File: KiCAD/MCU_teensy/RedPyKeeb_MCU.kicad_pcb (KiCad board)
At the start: 4 copper layers, 81 x 58 mm, 9 parts, among them J0 Conn_01x04, J1 Conn_02x20_Top_Bottom, J2 Conn_01x04, SW1 SW_DIP_x04, U0 Teensy4.1, U1 TXS0104ED

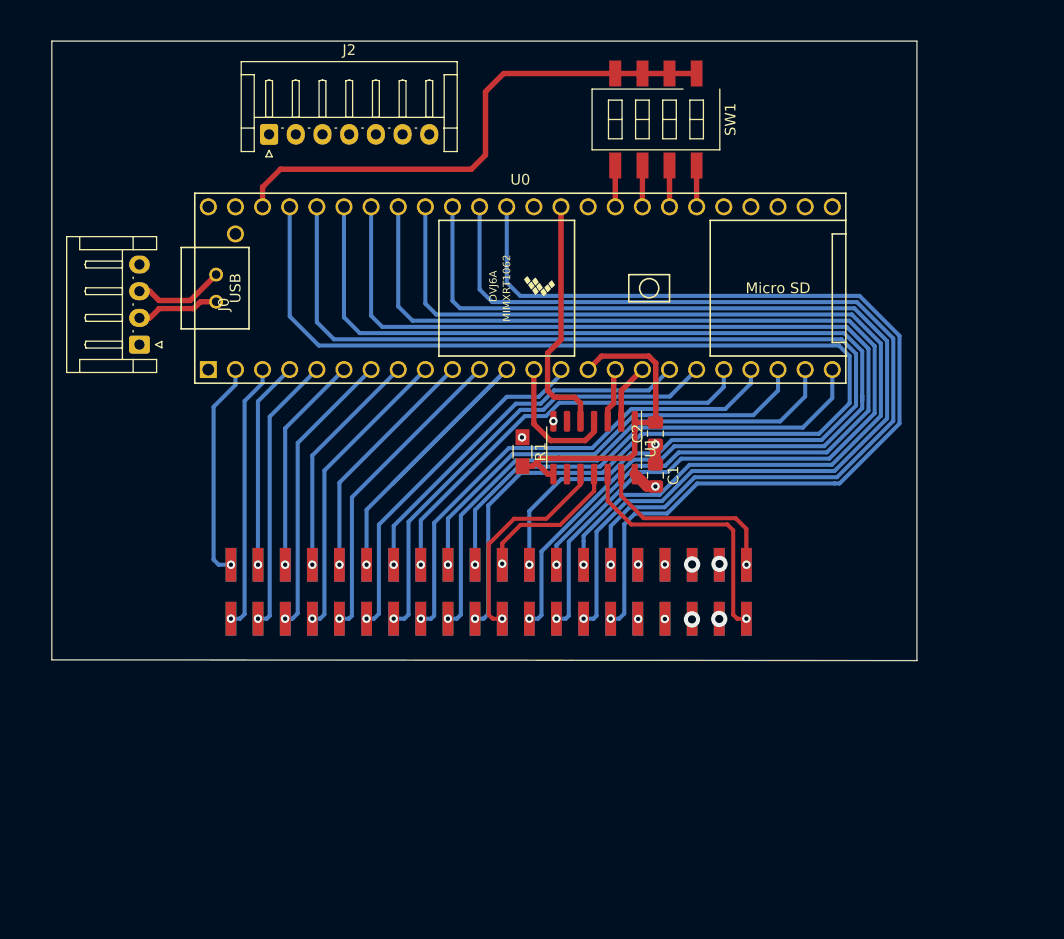
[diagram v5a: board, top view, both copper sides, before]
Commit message: Make more fixes and revisions to both PCBs, add in a pico for lighting and display functions and hook up an SPI bus with key event data.
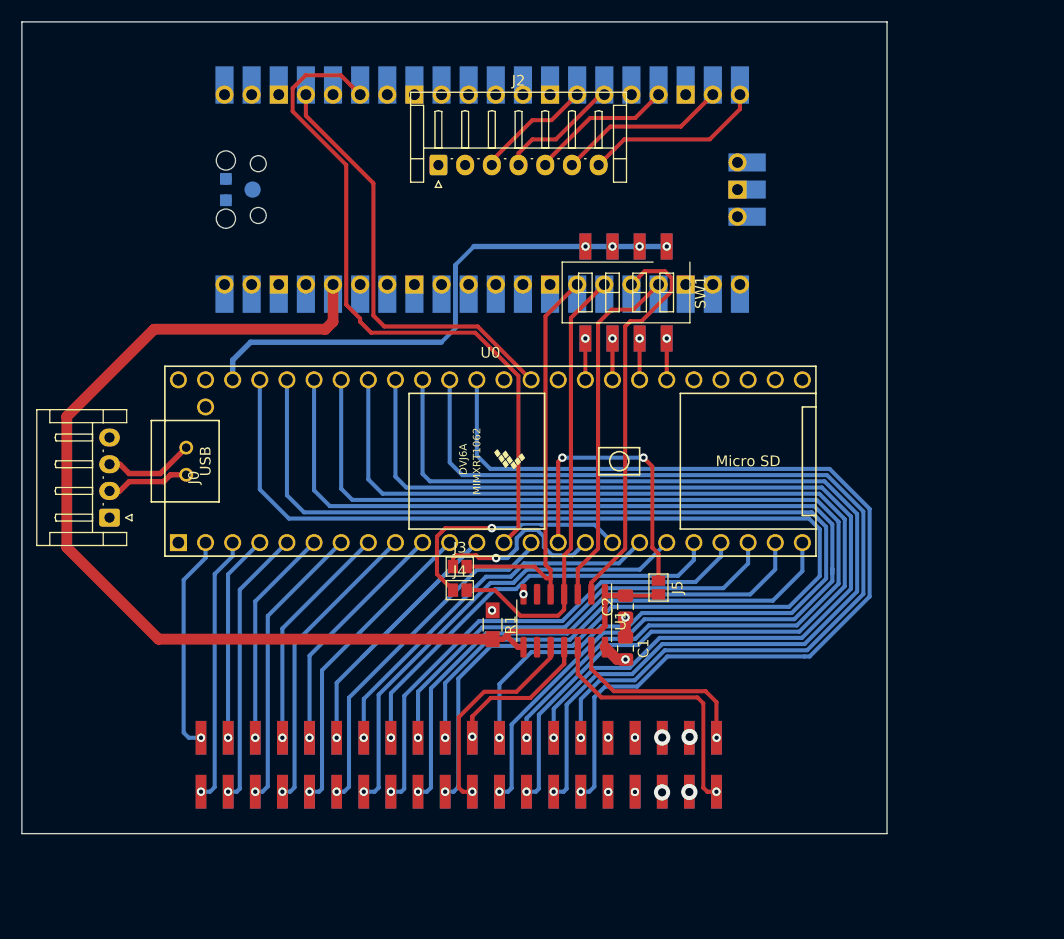
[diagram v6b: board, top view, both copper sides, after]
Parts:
- added J3: GS2, Connectors:GS2, F.Cu at (57.2, 66.2)
- added J4: GS2, Connectors:GS2, F.Cu at (57.2, 68.4)
- added J5: GS2, Connectors:GS2, F.Cu at (75.8, 68.2)
- added U2: Pico, Custom_pico:RPi_Pico_SMD_TH, B.Cu at (84.8, 20.4)
- SW1: footprint Buttons_Switches_SMD:SW_DIP_x4_W8.61mm_Slide_LowProfile -> Custom_pico:SW_DIP_x4_W8.61mm_Slide_LowProfile_bothsides
- moved C1 16.4 mm to (72.7, 73.9)
- moved J0 16.4 mm to (24.4, 61.6)
- moved J1 16.4 mm to (57.1, 84.8)
- moved R1 16.4 mm to (60.3, 71.6)
- moved U0 16.4 mm to (60.1, 56.3)
- moved U1 16.4 mm to (67.0, 71.3)
- moved SW1 16.4 mm to (72.8, 40.5)
- moved C2 16.4 mm to (72.7, 69.9)
- moved J2 16.1 mm to (55.2, 28.6)
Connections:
- C2 pad 2: 33_REF -> LED_33_REF
- R1 pad 2: 33_REF -> LED_33_REF
- U0 pad 13: LED_SDA_ROW0_MCU -> KEYS_MOSI
- U0 pad 16: LED_SCL_STATUS0_MCU -> Net-(J3-Pad1)
- U0 pad 17: LED_SDA_STATUS0_MCU -> Net-(J4-Pad1)
- U0 pad 35: LED_SCL_ROW0_MCU -> KEYS_CLK
- U0 pad 49: MAIN_VBUS -> Net-(U0-Pad49)
- U1 pad 1: 33_REF -> LED_33_REF
- U1 pad 8: 33_REF -> LED_33_REF
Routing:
- net LED_33_REF: track 0.00 -> 108.9 mm
- net KEYS_MOSI: track 0.00 -> 65.1 mm
- net KEYS_CLK: track 0.00 -> 40.6 mm
- net LED_SDA_STATUS0_MCU: track 5.66 -> 37.9 mm
- net LED_SDA_ROW0_MCU: track 12.7 -> 42.4 mm
- net LED_SCL_STATUS0_MCU: track 5.13 -> 33.3 mm
- net Net-(J4-Pad1): track 0.00 -> 23.2 mm, vias 0 -> 1
- net Net-(J3-Pad1): track 0.00 -> 17.1 mm, vias 0 -> 1
- net Net-(J2-Pad7): track 0.00 -> 16.8 mm
- net Net-(J2-Pad6): track 0.00 -> 15.9 mm
- net LED_SCL_ROW0_MCU: track 23.0 -> 38.7 mm
- net Net-(J2-Pad5): track 0.00 -> 13.5 mm
- net Net-(J2-Pad4): track 0.00 -> 11.4 mm
- net Net-(J2-Pad3): track 0.00 -> 11.0 mm
- net 33_REF_DIP: track 50.4 -> 56.3 mm, vias 0 -> 4
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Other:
- board size 81 x 58 mm -> 81 x 76 mm

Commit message: Allow for dual MCU for lighting/display and key management
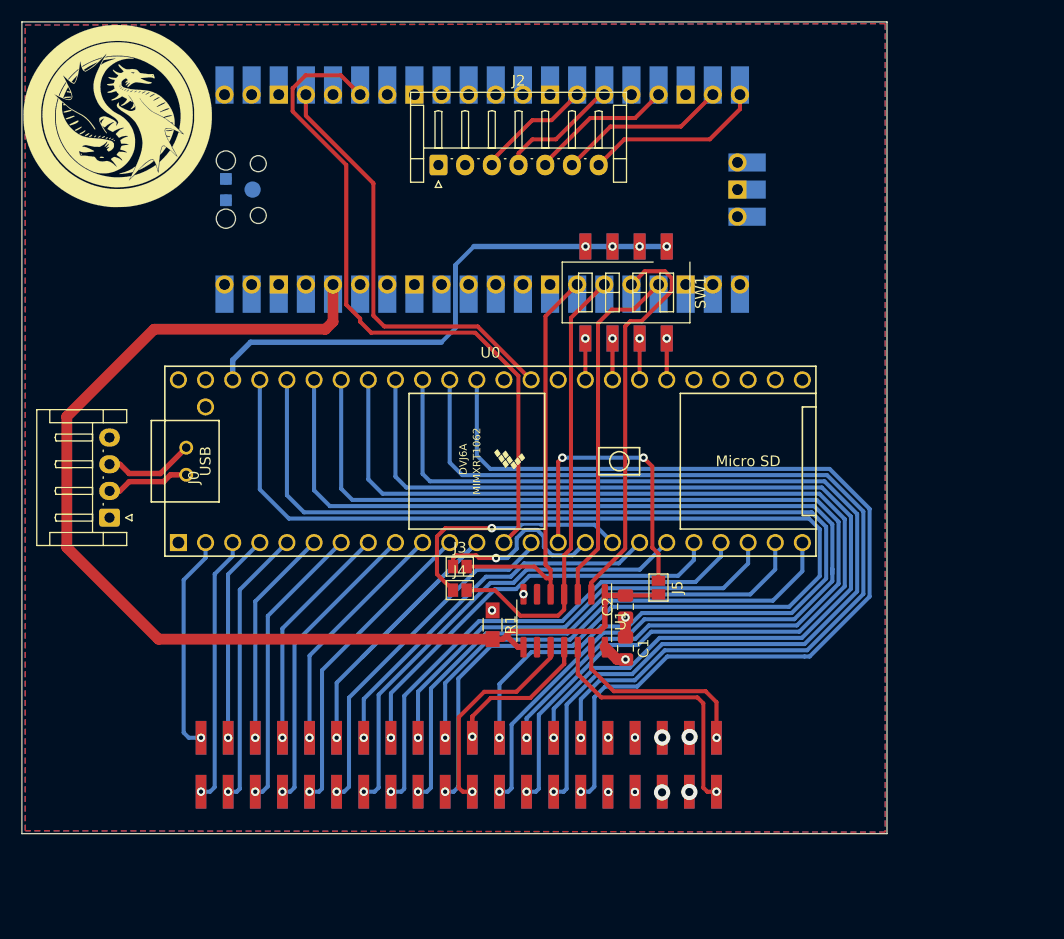
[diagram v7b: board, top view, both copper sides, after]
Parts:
- added G***: LOGO, Red_M.pretty:Red_M_20mm, F.Cu at (25.2, 24.0)
- added G***: LOGO, Red_M.pretty:Red_M_20mm, B.Cu at (25.2, 24.0)
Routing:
- added copper zone on B.Cu, net GNDPWR
- added copper zone on F.Cu, net GNDPWR
- added copper zone on In2.Cu, net GNDPWR
- added copper zone on In1.Cu, net MAIN_VBUS
- removed copper zone on GND, net GNDPWR
- removed copper zone on PWR, net MAIN_VBUS
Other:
- net class Default removed
- net class USB removed
